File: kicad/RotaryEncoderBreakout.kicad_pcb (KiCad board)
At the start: 2 copper layers, 33 x 34.3 mm, 17 parts, among them J1 Conn_01x04_Male, J2 Conn_01x04_Male, J3 Conn_01x05_Male, SW1 EC12PLRGB, U1 WS2811

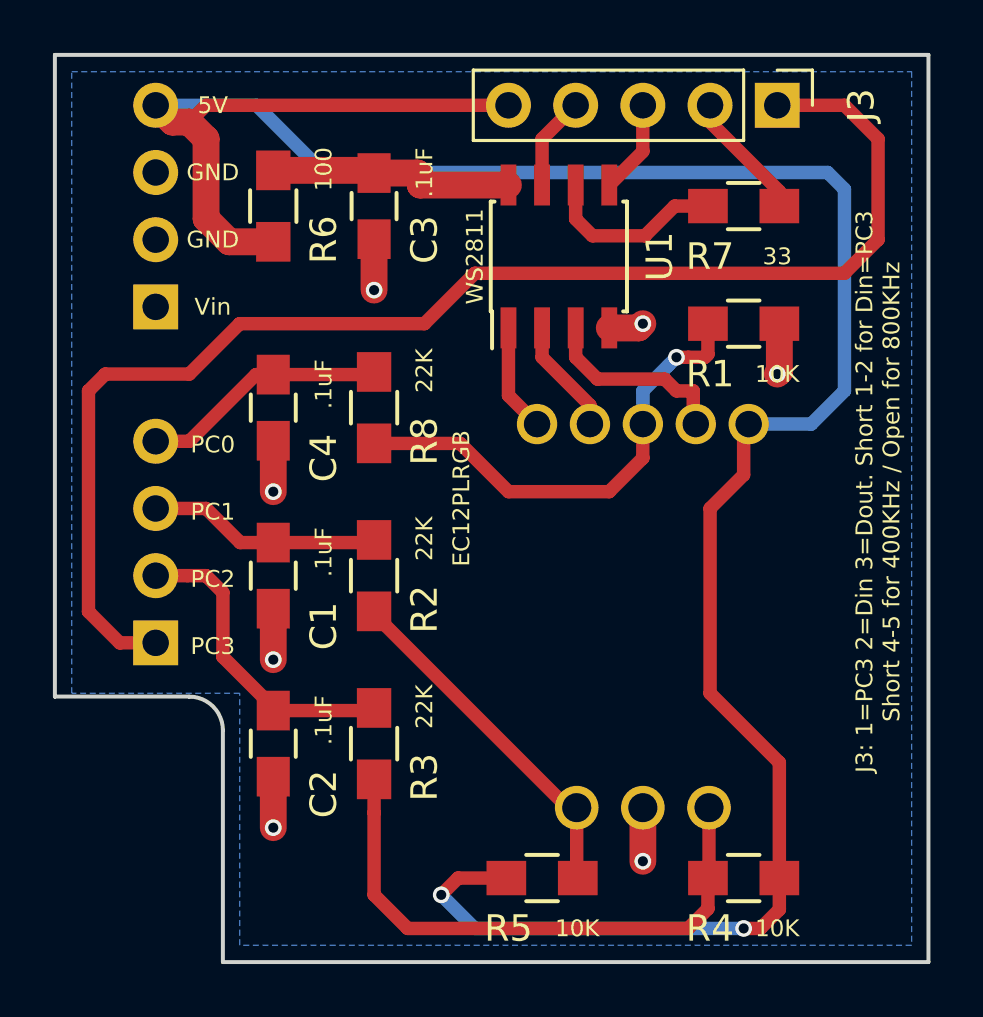
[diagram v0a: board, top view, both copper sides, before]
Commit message: Change J1 and J2 to socket headers
Change J1 & J2 from pin headers to Arduino-style socket strips.
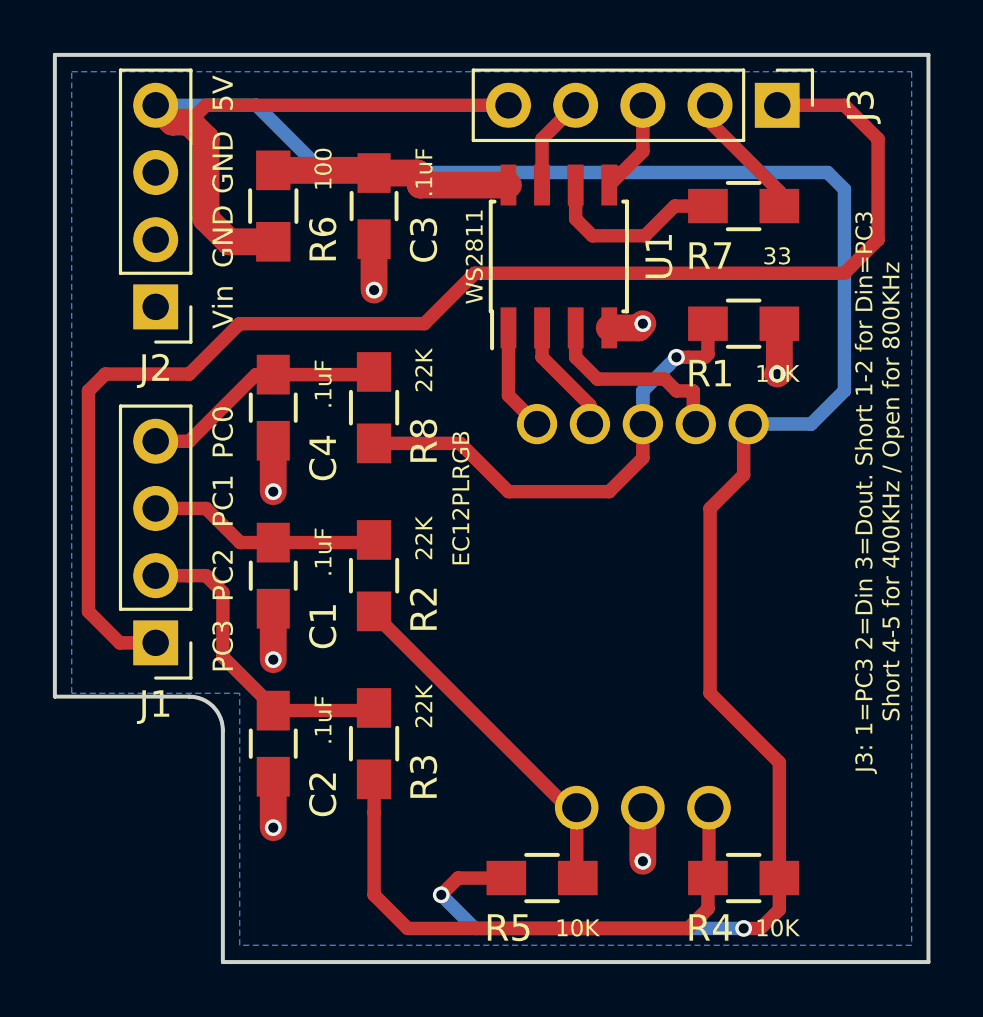
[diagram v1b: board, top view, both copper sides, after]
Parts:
- J1, J2: footprint lib_fp:Pin_Header_Straight_1x04_Pitch2.54mm -> lib_fp:Socket_Strip_Straight_1x04_Pitch2.54mm; moved to F.Cu
- turned J1 to 180 degrees
- turned J2 to 180 degrees
